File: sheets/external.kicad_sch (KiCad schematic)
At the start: 5 parts, among them CN3 STE_I2C_QT, M1 Motor_Servo, M2 Motor_Servo

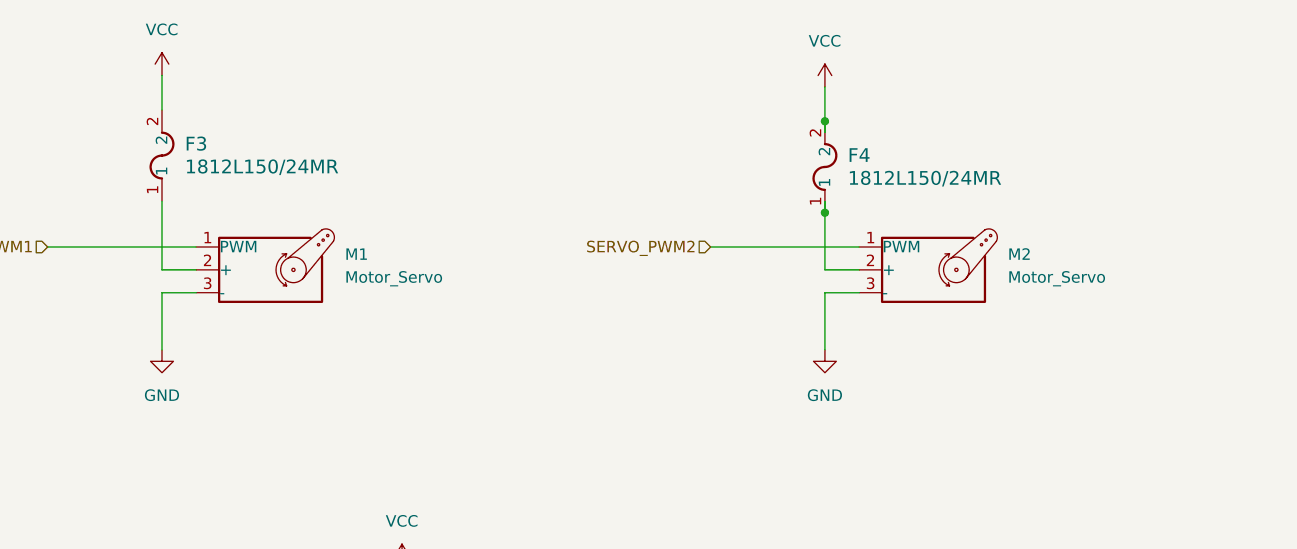
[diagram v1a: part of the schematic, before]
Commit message: Added NEOM9N breakout symbol
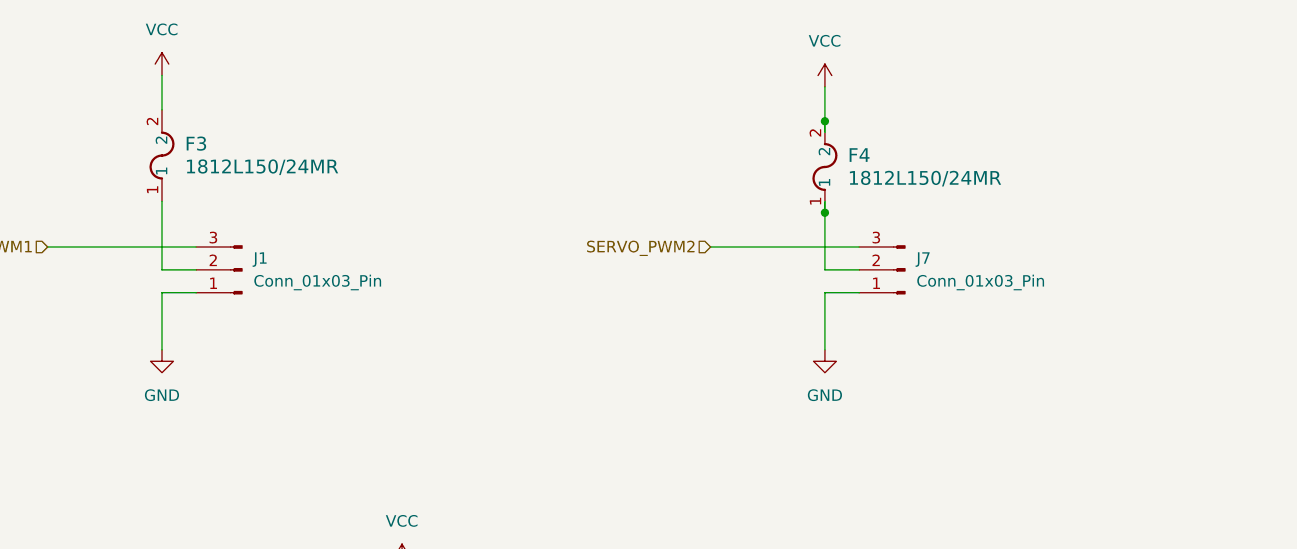
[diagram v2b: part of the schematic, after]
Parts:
- removed M1, M2: Motor_Servo, symbol Motor:Motor_Servo
- added J1, J7: Conn_01x03_Pin, symbol Connector:Conn_01x03_Pin
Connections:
- net GND: now also J1.1 (Pin_1), J7.1 (Pin_1)
- net SERVO_PWM1: now also J1.3 (Pin_3)
- net SERVO_PWM2: now also J7.3 (Pin_3)
- net at F4.1: now also J7.2 (Pin_2)
- net at F3.1: now also J1.2 (Pin_2)
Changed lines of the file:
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@@
-	(wire
-		(pts
-			(xy 43.18 46.99) (xy 39.37 46.99)
-		)
-		(stroke
-			(width 0)
-			(type default)
-		)
-	)
 	(wire
 		(pts
@@
 		(pts
 			(xy 39.37 44.45) (xy 43.18 44.45)
+		)
+		(stroke
+			(width 0)
+			(type default)
+		)
+	)
+	(wire
+		(pts
+			(xy 39.37 46.99) (xy 43.18 46.99)
 		)
 		(stroke
@@
 	)
 	(symbol
-		(lib_id "Motor:Motor_Servo")
-		(at 50.8 44.45 0)
-		(unit 1)
-		(exclude_from_sim no)
-		(in_bom yes)
-		(on_board yes)
-		(dnp no)
-		(fields_autoplaced yes)
-		(property "Reference" "M1"
-			(at 59.69 42.7468 0)
-			(effects
-				(font
-					(size 1.27 1.27)
-				)
-				(justify left)
-			)
-		)
-		(property "Value" "Motor_Servo"
-			(at 59.69 45.2868 0)
-			(effects
-				(font
-					(size 1.27 1.27)
-				)
-				(justify left)
-			)
-		)
-		(property "Footprint" ""
-			(at 50.8 49.276 0)
-			(effects
-				(font
-					(size 1.27 1.27)
-				)
-				(hide yes)
-			)
-		)
-		(property "Datasheet" "http://forums.parallax.com/uploads/attachments/46831/74481.png"
-			(at 50.8 49.276 0)
-			(effects
-				(font
-					(size 1.27 1.27)
-				)
-				(hide yes)
-			)
-		)
-		(property "Description" "Servo Motor (Futaba, HiTec, JR connector)"
-			(at 50.8 44.45 0)
-			(effects
-				(font
-					(size 1.27 1.27)
-				)
-				(hide yes)
-			)
-		)
-		(pin "2"
-		)
-		(pin "3"
-		)
-		(pin "1"
-		)
-		(instances
-			(project "aerolotl"
-				(path "/3f5bc5ea-feaa-4ed9-b0e0-c918b1fb5754/5f72b0ed-0324-499f-bb98-18e31eb15f1d"
-					(reference "M1")
-					(unit 1)
-				)
-			)
-		)
-	)
-	(symbol
 		(lib_id "power:GND")
 		(at 113.03 53.34 0)
@@
 	)
 	(symbol
-		(lib_id "Motor:Motor_Servo")
-		(at 124.46 44.45 0)
+		(lib_id "Connector:Conn_01x03_Pin")
+		(at 48.26 44.45 180)
 		(unit 1)
 		(exclude_from_sim no)
@@
 		(dnp no)
 		(fields_autoplaced yes)
-		(property "Reference" "M2"
-			(at 133.35 42.7468 0)
-			(effects
-				(font
-					(size 1.27 1.27)
-				)
-				(justify left)
-			)
-		)
-		(property "Value" "Motor_Servo"
-			(at 133.35 45.2868 0)
-			(effects
-				(font
-					(size 1.27 1.27)
-				)
-				(justify left)
+		(property "Reference" "J1"
+			(at 49.53 43.1799 0)
+			(effects
+				(font
+					(size 1.27 1.27)
+				)
+				(justify right)
+			)
+		)
+		(property "Value" "Conn_01x03_Pin"
+			(at 49.53 45.7199 0)
+			(effects
+				(font
+					(size 1.27 1.27)
+				)
+				(justify right)
 			)
 		)
 		(property "Footprint" ""
-			(at 124.46 49.276 0)
-			(effects
-				(font
-					(size 1.27 1.27)
-				)
-				(hide yes)
-			)
-		)
-		(property "Datasheet" "http://forums.parallax.com/uploads/attachments/46831/74481.png"
-			(at 124.46 49.276 0)
-			(effects
-				(font
-					(size 1.27 1.27)
-				)
-				(hide yes)
-			)
-		)
-		(property "Description" "Servo Motor (Futaba, HiTec, JR connector)"
-			(at 124.46 44.45 0)
+			(at 48.26 44.45 0)
+			(effects
+				(font
+					(size 1.27 1.27)
+				)
+				(hide yes)
+			)
+		)
+		(property "Datasheet" "~"
+			(at 48.26 44.45 0)
+			(effects
+				(font
+					(size 1.27 1.27)
+				)
+				(hide yes)
+			)
+		)
+		(property "Description" "Generic connector, single row, 01x03, script generated"
+			(at 48.26 44.45 0)
 			(effects
 				(font
@@
 		)
 		(instances
-			(project "aerolotl"
+			(project ""
 				(path "/3f5bc5ea-feaa-4ed9-b0e0-c918b1fb5754/5f72b0ed-0324-499f-bb98-18e31eb15f1d"
-					(reference "M2")
+					(reference "J1")
 					(unit 1)
 				)
@@
 					(unit 1)
 				)
+			)
+		)
+	)
+	(symbol
+		(lib_id "Connector:Conn_01x03_Pin")
+		(at 121.92 44.45 180)
+		(unit 1)
+		(exclude_from_sim no)
+		(in_bom yes)
+		(on_board yes)
+		(dnp no)
+		(fields_autoplaced yes)
+		(property "Reference" "J7"
+			(at 123.19 43.1799 0)
+			(effects
+				(font
+					(size 1.27 1.27)
+				)
+				(justify right)
+			)
+		)
+		(property "Value" "Conn_01x03_Pin"
+			(at 123.19 45.7199 0)
+			(effects
+				(font
+					(size 1.27 1.27)
+				)
+				(justify right)
+			)
+		)
+		(property "Footprint" ""
+			(at 121.92 44.45 0)
+			(effects
+				(font
+					(size 1.27 1.27)
+				)
+				(hide yes)
+			)
+		)
+		(property "Datasheet" "~"
+			(at 121.92 44.45 0)
+			(effects
+				(font
+					(size 1.27 1.27)
+				)
+				(hide yes)
+			)
+		)
+		(property "Description" "Generic connector, single row, 01x03, script generated"
+			(at 121.92 44.45 0)
+			(effects
+				(font
+					(size 1.27 1.27)
+				)
+				(hide yes)
+			)
+		)
+		(pin "2"
+		)
+		(pin "3"
+		)
+		(pin "1"
+		)
+		(instances
+			(project "aerolotl"
+				(path "/3f5bc5ea-feaa-4ed9-b0e0-c918b1fb5754/5f72b0ed-0324-499f-bb98-18e31eb15f1d"
+					(reference "J7")
+					(unit 1)
+				)

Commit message: Fixed up power, added remaining to do
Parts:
- removed J1, J7: Conn_01x03_Pin, symbol Connector:Conn_01x03_Pin
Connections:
- net NEOM9N.SCL renamed EXT_I2C.SCL
- net NEOM9N.SDA renamed EXT_I2C.SDA
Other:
- note added: "To-do - Add TPS54620 circuit for managing power (or external BEC)"
- note removed: "To-do - Connect 2 Servo PWM channels -> DONE (from lawton) - Qwic connector with I2C peripheral -> DONE (from lawton) - SPI peripheral connector -> IN PROGRESS - Standard 0.1" header pinout - Transceiver output"
- moved on the sheet: F4
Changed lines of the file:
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@@
 	(generator_version "9.0")
 	(paper "A4")
-	(text "To-do \n- Connect 2 Servo PWM channels \n	-> DONE (from lawton)\n- Qwic connector with I2C peripheral\n	-> DONE (from lawton)\n- SPI peripheral connector\n	-> IN PROGRESS\n- Standard 0.1\" header pinout\n- Transceiver output\n"
+	(text "To-do \n- Add TPS54620 circuit for managing power (or external BEC)\n"
 		(exclude_from_sim no)
-		(at 123.444 88.138 0)
+		(at 46.99 45.72 0)
 		(effects
 			(font
@@
 	)
 	(junction
-		(at 113.03 27.94)
+		(at 134.62 29.21)
 		(diameter 0)
 		(color 0 0 0 0)
@@
 	)
 	(junction
-		(at 113.03 38.1)
+		(at 134.62 39.37)
 		(diameter 0)
 		(color 0 0 0 0)
@@
 	(wire
 		(pts
-			(xy 113.03 44.45) (xy 116.84 44.45)
+			(xy 134.62 45.72) (xy 138.43 45.72)
+		)
+		(stroke
+			(width 0)
+			(type default)
+		)
+	)
+	(wire
+		(pts
+			(xy 50.8 87.63) (xy 71.12 87.63)
 		)
 		(stroke
@@
 	(wire
 		(pts
-			(xy 100.33 41.91) (xy 116.84 41.91)
+			(xy 121.92 43.18) (xy 138.43 43.18)
 		)
 		(stroke
@@
 	(wire
 		(pts
-			(xy 113.03 38.1) (xy 113.03 44.45)
+			(xy 134.62 39.37) (xy 134.62 45.72)
 		)
 		(stroke
@@
 	(wire
 		(pts
-			(xy 113.03 36.83) (xy 113.03 38.1)
+			(xy 134.62 38.1) (xy 134.62 39.37)
 		)
 		(stroke
@@
 	(wire
 		(pts
-			(xy 113.03 27.94) (xy 113.03 29.21)
-		)
-		(stroke
-			(width 0)
-			(type default)
-		)
-	)
-	(wire
-		(pts
-			(xy 113.03 24.13) (xy 113.03 27.94)
-		)
-		(stroke
-			(width 0)
-			(type default)
-		)
-	)
-	(wire
-		(pts
-			(xy 116.84 46.99) (xy 113.03 46.99)
+			(xy 134.62 29.21) (xy 134.62 30.48)
+		)
+		(stroke
+			(width 0)
+			(type default)
+		)
+	)
+	(wire
+		(pts
+			(xy 134.62 25.4) (xy 134.62 29.21)
+		)
+		(stroke
+			(width 0)
+			(type default)
+		)
+	)
+	(wire
+		(pts
+			(xy 138.43 48.26) (xy 134.62 48.26)
 		)
 		(stroke
@@
 		)
 	)
-	(wire
-		(pts
-			(xy 50.8 87.63) (xy 71.12 87.63)
+	(bus
+		(pts
+			(xy 48.26 85.09) (xy 48.26 87.63)
 		)
 		(stroke
@@
 	(bus
 		(pts
-			(xy 48.26 85.09) (xy 48.26 87.63)
-		)
-		(stroke
-			(width 0)
-			(type default)
-		)
-	)
-	(bus
-		(pts
 			(xy 48.26 82.55) (xy 48.26 85.09)
 		)
@@
 	(wire
 		(pts
-			(xy 113.03 46.99) (xy 113.03 53.34)
+			(xy 134.62 48.26) (xy 134.62 54.61)
 		)
 		(stroke
@@
 		)
 	)
-	(label "NEOM9N.SCL"
+	(label "EXT_I2C.SCL"
 		(at 50.8 90.17 0)
 		(effects
@@
 		)
 	)
-	(label "NEOM9N.SDA"
+	(label "EXT_I2C.SDA"
 		(at 50.8 87.63 0)
 		(effects
@@
 		)
 	)
-	(hierarchical_label "EXTERNAL{SDA, SCL}"
+	(hierarchical_label "EXT_I2C{SDA, SCL}"
 		(shape bidirectional)
 		(at 48.26 82.55 180)
@@
 	(hierarchical_label "SERVO_PWM2"
 		(shape input)
-		(at 100.33 41.91 180)
+		(at 121.92 43.18 180)
 		(effects
 			(font
@@
 	(symbol
 		(lib_id "aerolotl_custom:1812L150_PTC_Fuse")
-		(at 113.03 38.1 90)
+		(at 134.62 39.37 90)
 		(unit 1)
 		(exclude_from_sim no)
@@
 		(fields_autoplaced yes)
 		(property "Reference" "F4"
-			(at 115.57 31.7499 90)
+			(at 137.16 33.0199 90)
 			(effects
 				(font
@@
 		)
 		(property "Value" "1812L150/24MR"
-			(at 115.57 34.2899 90)
+			(at 137.16 35.5599 90)
 			(effects
 				(font
@@
 		)
 		(property "Footprint" "aerolotl_custom:FUSE_1812L150&slash_24_LTF"
-			(at 113.03 38.1 0)
+			(at 134.62 39.37 0)
 			(effects
 				(font
@@
 		)
 		(property "Datasheet" "1812L150/24MR"
-			(at 113.03 38.1 0)
+			(at 134.62 39.37 0)
 			(effects
 				(font
@@
 		)
 		(property "Description" ""
-			(at 113.03 38.1 0)
+			(at 134.62 39.37 0)
 			(effects
 				(font
@@
 	(symbol
 		(lib_id "power:GND")
-		(at 113.03 53.34 0)
+		(at 134.62 54.61 0)
 		(unit 1)
 		(exclude_from_sim no)
@@
 		(fields_autoplaced yes)
 		(property "Reference" "#PWR085"
-			(at 113.03 59.69 0)
+			(at 134.62 60.96 0)
 			(effects
 				(font
@@
 		)
 		(property "Value" "GND"
-			(at 113.03 58.42 0)
+			(at 134.62 59.69 0)
 			(effects
 				(font
@@
 		)
 		(property "Footprint" ""
-			(at 113.03 53.34 0)
+			(at 134.62 54.61 0)
 			(effects
 				(font
@@
 		)
 		(property "Datasheet" ""
-			(at 113.03 53.34 0)
+			(at 134.62 54.61 0)
 			(effects
 				(font
@@
 		)
 		(property "Description" "Power symbol creates a global label with name \"GND\" , ground"
-			(at 113.03 53.34 0)
+			(at 134.62 54.61 0)
 			(effects
 				(font
@@
 	)
 	(symbol
-		(lib_id "Connector:Conn_01x03_Pin")
-		(at 48.26 44.45 180)
-		(unit 1)
-		(exclude_from_sim no)
-		(in_bom yes)
-		(on_board yes)
-		(dnp no)
-		(fields_autoplaced yes)
-		(property "Reference" "J1"
-			(at 49.53 43.1799 0)
-			(effects
-				(font
-					(size 1.27 1.27)
-				)
-				(justify right)
-			)
-		)
-		(property "Value" "Conn_01x03_Pin"
-			(at 49.53 45.7199 0)
-			(effects
-				(font
-					(size 1.27 1.27)
-				)
-				(justify right)
-			)
-		)
-		(property "Footprint" ""
-			(at 48.26 44.45 0)
-			(effects
-				(font
-					(size 1.27 1.27)
-				)
-				(hide yes)
-			)
-		)
-		(property "Datasheet" "~"
-			(at 48.26 44.45 0)
-			(effects
-				(font
-					(size 1.27 1.27)
-				)
-				(hide yes)
-			)
-		)
-		(property "Description" "Generic connector, single row, 01x03, script generated"
-			(at 48.26 44.45 0)
-			(effects
-				(font
-					(size 1.27 1.27)
-				)
-				(hide yes)
-			)
-		)
-		(pin "2"
-		)
-		(pin "3"
-		)
-		(pin "1"
-		)
-		(instances
-			(project ""
-				(path "/3f5bc5ea-feaa-4ed9-b0e0-c918b1fb5754/5f72b0ed-0324-499f-bb98-18e31eb15f1d"
-					(reference "J1")
-					(unit 1)
-				)
-			)
-		)
-	)
-	(symbol
 		(lib_id "power:VCC")
 		(at 66.04 77.47 0)
@@
 				(path "/3f5bc5ea-feaa-4ed9-b0e0-c918b1fb5754/5f72b0ed-0324-499f-bb98-18e31eb15f1d"
 					(reference "#PWR082")
-					(unit 1)
-				)
-			)
-		)
-	)
-	(symbol
-		(lib_id "Connector:Conn_01x03_Pin")
-		(at 121.92 44.45 180)
-		(unit 1)
-		(exclude_from_sim no)
-		(in_bom yes)
-		(on_board yes)
-		(dnp no)
-		(fields_autoplaced yes)
-		(property "Reference" "J7"
-			(at 123.19 43.1799 0)
-			(effects
-				(font
-					(size 1.27 1.27)
-				)
-				(justify right)
-			)
-		)
-		(property "Value" "Conn_01x03_Pin"
-			(at 123.19 45.7199 0)
-			(effects
-				(font
-					(size 1.27 1.27)
-				)
-				(justify right)
-			)
-		)
-		(property "Footprint" ""
-			(at 121.92 44.45 0)
-			(effects
-				(font
-					(size 1.27 1.27)
-				)
-				(hide yes)
-			)
-		)
-		(property "Datasheet" "~"
-			(at 121.92 44.45 0)
-			(effects
-				(font
-					(size 1.27 1.27)
-				)
-				(hide yes)
-			)
-		)
-		(property "Description" "Generic connector, single row, 01x03, script generated"
-			(at 121.92 44.45 0)
-			(effects
-				(font
-					(size 1.27 1.27)
-				)
-				(hide yes)
-			)
-		)
-		(pin "2"
-		)
-		(pin "3"
-		)
-		(pin "1"
-		)
-		(instances
-			(project "aerolotl"
-				(path "/3f5bc5ea-feaa-4ed9-b0e0-c918b1fb5754/5f72b0ed-0324-499f-bb98-18e31eb15f1d"
-					(reference "J7")
 					(unit 1)
 				)
@@
 	(symbol
 		(lib_id "power:VCC")
-		(at 113.03 24.13 0)
+		(at 134.62 25.4 0)
 		(unit 1)
 		(exclude_from_sim no)
@@
 		(fields_autoplaced yes)
 		(property "Reference" "#PWR084"
-			(at 113.03 27.94 0)
+			(at 134.62 29.21 0)
 			(effects
 				(font
@@
 		)
 		(property "Value" "VCC"
-			(at 113.03 19.05 0)
+			(at 134.62 20.32 0)
 			(effects
 				(font
@@
 		)
 		(property "Footprint" ""
-			(at 113.03 24.13 0)
+			(at 134.62 25.4 0)
 			(effects
 				(font
@@
 		)
 		(property "Datasheet" ""
-			(at 113.03 24.13 0)
+			(at 134.62 25.4 0)
 			(effects
 				(font
@@
 		)
 		(property "Description" "Power symbol creates a global label with name \"VCC\""
-			(at 113.03 24.13 0)
-			(effects
-				(font
+			(at 134.62 25.4 0)
+			(effects
+				(font
